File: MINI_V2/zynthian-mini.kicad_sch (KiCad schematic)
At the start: 87 parts, among them J1 NEUTRIK, SW1 SW_Push, SW10 SW_Push, SW11 SW_Push, SW12 SW_Push, SW13 SW_Push, SW14 SW_Push, SW15 SW_Push, SW16 SW_Push, SW17 SW_Push, SW18 SW_Push, SW19 SW_Push, SW2 SW_Push, SW20 SW_Push, SW3 SW_Push, SW4 SW_Push, SW5 SW_Push, SW6 SW_Push, SW7 SW_Push, SW8 SW_Push, SW9 SW_Push, U1 74HCT14, U2 H11L1M

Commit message: removed PCM sound card, resized pin connector from 3 to 6 pins
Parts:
- removed A1: GY-PCM5102, project-footprints:GY-PCM5102, symbol gy-pcm5102:GY-PCM5102
- removed C3: 100n, project-footprints:C_Rect_L7.0mm_W2.0mm_P5.00mm, symbol Device:C
- removed C4: 100u, Capacitor_THT:CP_Radial_D6.3mm_P2.50mm, symbol Device:C_Polarized
- stereo_conn_01: symbol Connector:Conn_01x03_Pin -> Connector:Conn_01x06_Pin
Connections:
- net AUDIO_GND_OUT: now also stereo_conn_01.3 (Pin_3); no longer stereo_conn_01.2 (Pin_2)
- net AUDIO_L_OUT: now also stereo_conn_01.4 (Pin_4); no longer stereo_conn_01.3 (Pin_3)
- net AUDIO_R_OUT: now also stereo_conn_01.2 (Pin_2); no longer stereo_conn_01.1 (Pin_1)
- no-connect marks 18 -> 12

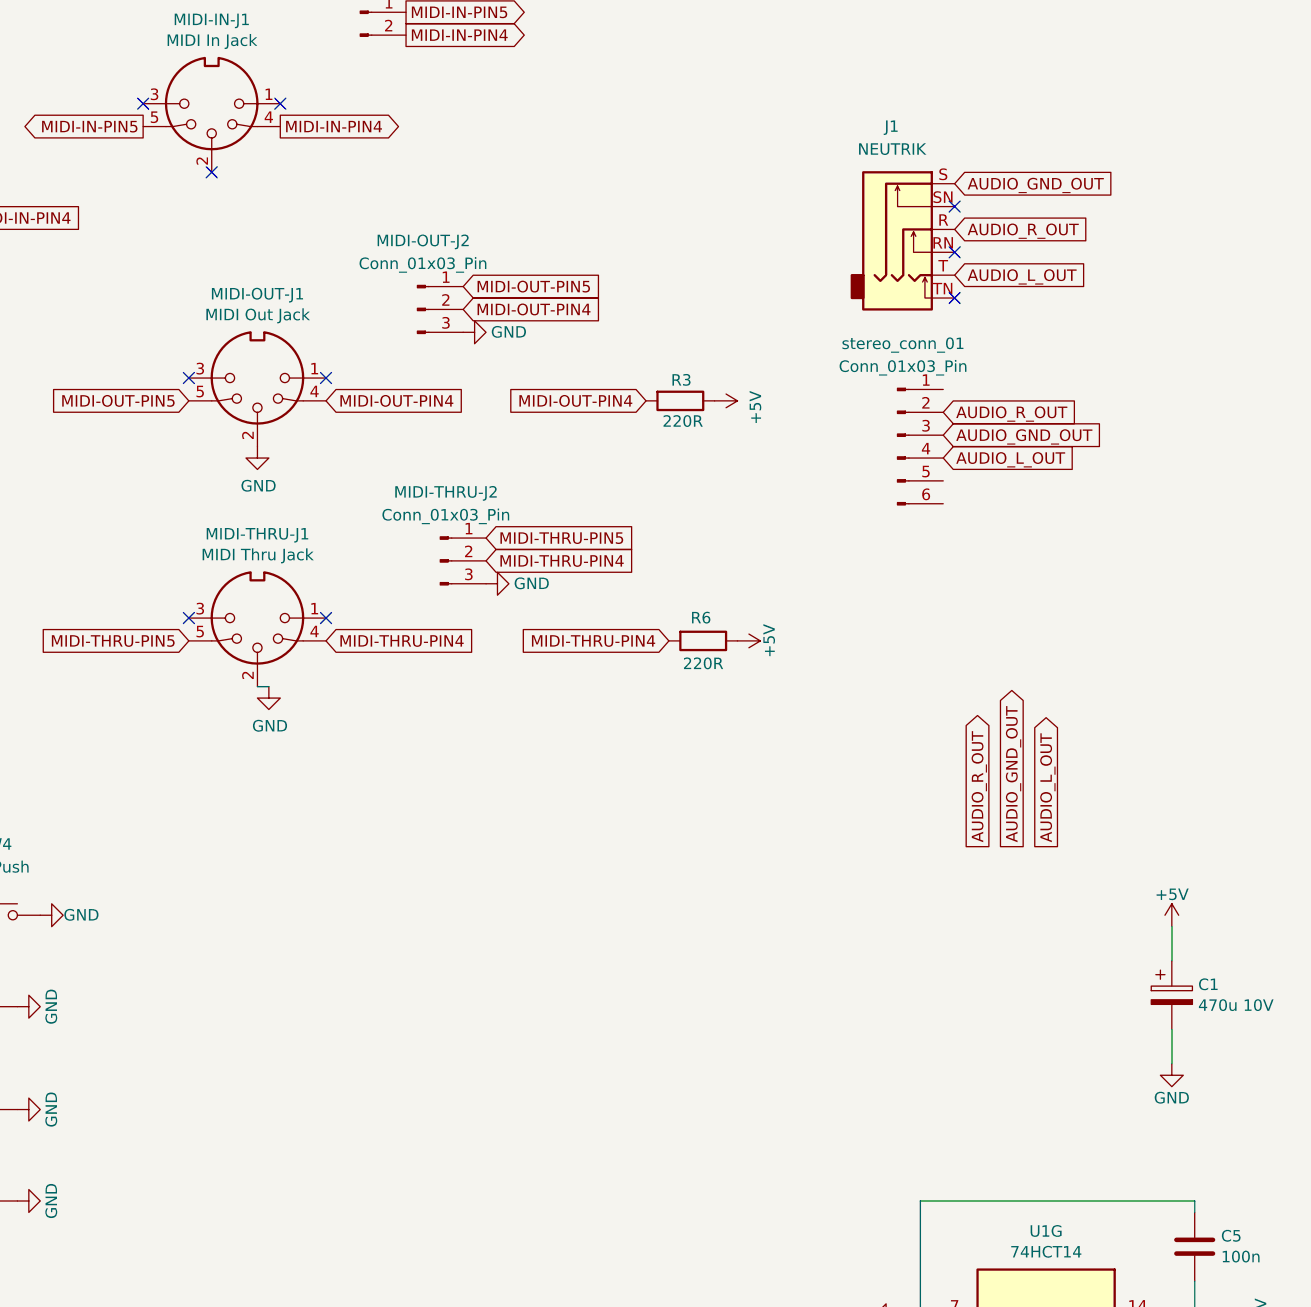
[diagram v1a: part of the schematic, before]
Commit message: 2x6.3 connectors done, trying one mini jack
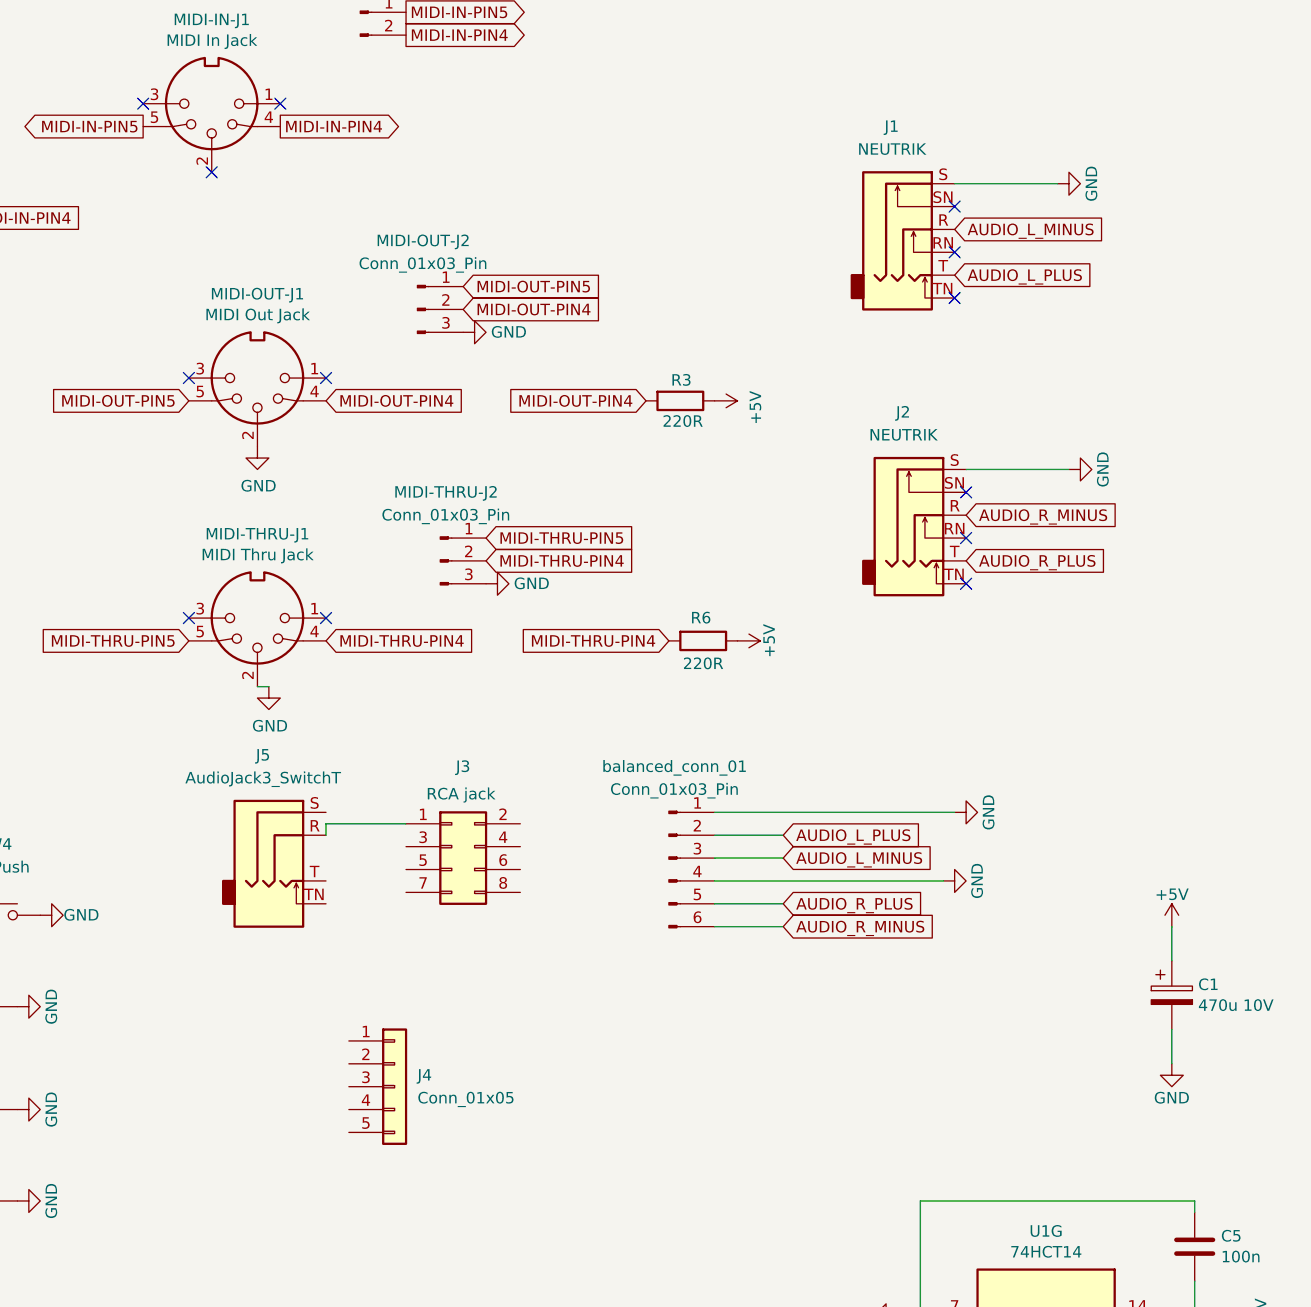
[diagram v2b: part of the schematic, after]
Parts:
- added J2: NEUTRIK, project-footprints:Jack_6.35mm_Neutrik_NMJ6HFD2_Horizontal, symbol Connector_Audio:NMJ6HFD2
- added J3: Conn_02x04_Odd_Even, Connector_PinHeader_2.54mm:PinHeader_2x04_P2.54mm_Vertical, symbol Connector_Generic:Conn_02x04_Odd_Even
- added J4: Conn_01x05, Connector_PinHeader_2.54mm:PinHeader_1x05_P2.54mm_Vertical, symbol Connector_Generic:Conn_01x05
- added J5: AudioJack3_SwitchT, Connector_Audio:Jack_3.5mm_KoreanHropartsElec_PJ-320D-4A_Horizontal, symbol Connector_Audio:AudioJack3_SwitchT
- balanced_conn_01: renamed from stereo_conn_01; footprint Connector_PinHeader_2.54mm:PinHeader_1x03_P2.54mm_Vertical -> Connector_PinHeader_2.54mm:PinHeader_1x06_P2.54mm_Vertical
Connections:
- net GND: now also J1.S, balanced_conn_01.1 (Pin_1), balanced_conn_01.4 (Pin_4), J2.S
- net AUDIO_R_PLUS: now reaches balanced_conn_01.5 (Pin_5)
- net AUDIO_R_PLUS: now also J2.T
- net AUDIO_R_MINUS: now reaches balanced_conn_01.6 (Pin_6)
- net AUDIO_R_MINUS: now also J2.R
- net AUDIO_GND_OUT renamed AUDIO_L_MINUS
- net AUDIO_L_MINUS: now also J1.R; no longer J1.S
- net AUDIO_L_OUT renamed AUDIO_L_PLUS
- net AUDIO_L_PLUS: now also balanced_conn_01.2 (Pin_2); no longer balanced_conn_01.4 (Pin_4)
- removed net AUDIO_R_OUT: J1.R, balanced_conn_01.2 (Pin_2)
- new net: J3.1 (Pin_1), J5.R
- no-connect marks 12 -> 15
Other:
- moved on the sheet: balanced_conn_01

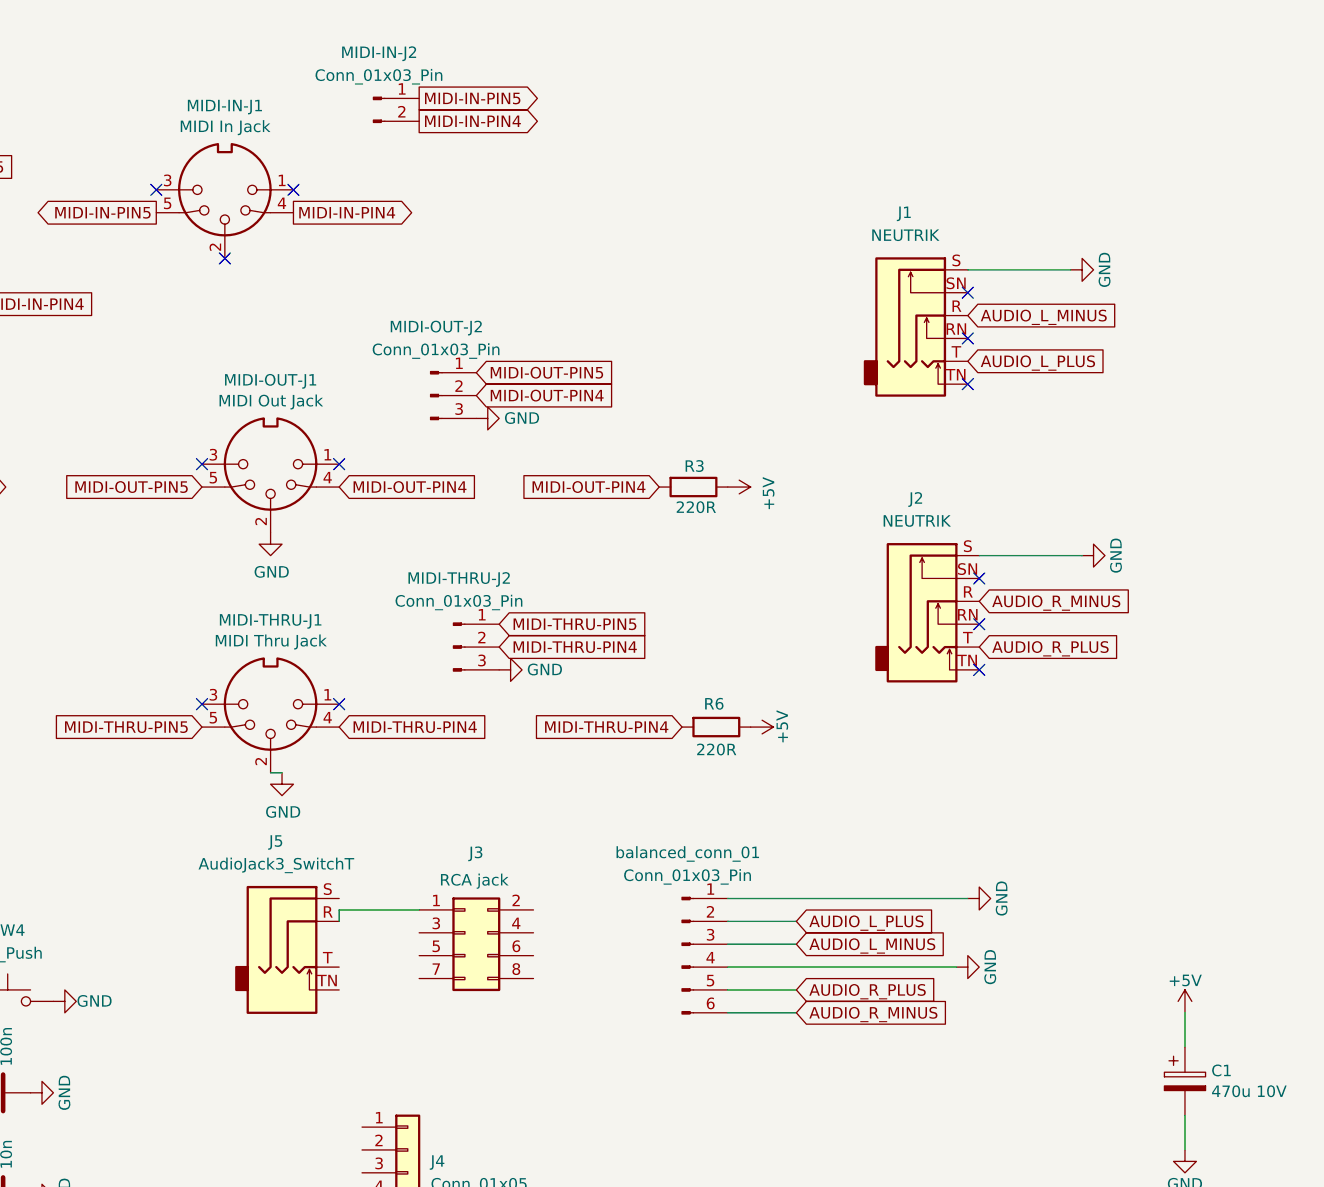
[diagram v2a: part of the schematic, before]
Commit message: add TRRS jack symbol and footprint, connect to line out
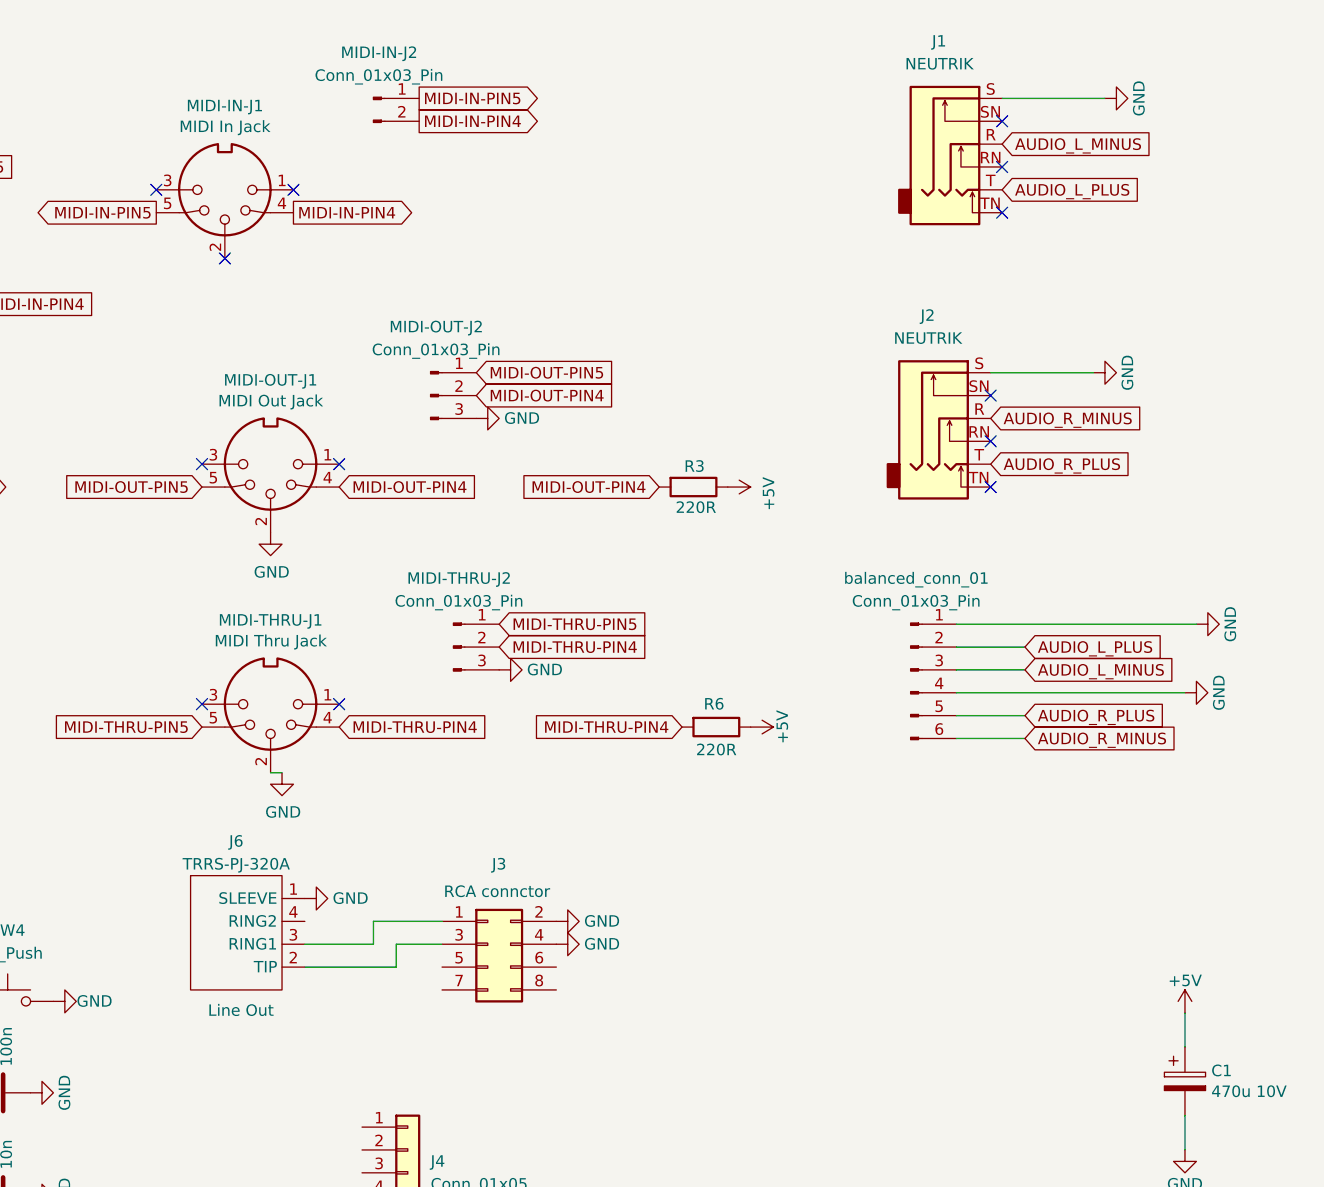
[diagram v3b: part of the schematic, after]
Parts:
- removed J5: AudioJack3_SwitchT, Connector_Audio:Jack_3.5mm_KoreanHropartsElec_PJ-320D-4A_Horizontal, symbol Connector_Audio:AudioJack3_SwitchT
- added J6: TRRS-PJ-320A, project-footprints:TRRS-PJ-320A, symbol TRRS_jack:TRRS-PJ-320A
- J3: Comment RCA jack -> RCA connctor
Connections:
- net GND: now also J3.2 (Pin_2), J3.4 (Pin_4), J6.1 (SLEEVE)
- net at J3.1 (Pin_1): now also J6.3 (RING1)
- net at J3.3 (Pin_3): now also J6.2 (TIP)
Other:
- moved on the sheet: J1, J2, J3, balanced_conn_01
